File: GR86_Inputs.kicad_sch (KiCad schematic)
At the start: 57 parts, among them U801 74LV1T125, U802 74LV1T125, U803 74LV1T125, U804 74LV1T125, U805 74LV1T125, U806 ES7241D

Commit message: Update .gitignore, CANBus_Interface.kicad_sch, ESP32-S3_WLED_UnderGlow_Hat-2026-05-04_233126.zip, and 17 more files
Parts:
- removed C811, C816: 22uF, My Capacitors:C_0603_Dense, symbol Device:C_Small
- removed C812, C813, C815, C818, C821: 0.1uF, My Capacitors:C_0201_Dense, symbol Device:C_Small
- removed C814, C817, C819, C820, C822: 1uF, My Capacitors:C_0402_Dense, symbol Device:C_Small
- added C811, C816: 22uF, My Capacitors:C_0603_Dense, symbol Device:C
- added C812, C813, C815, C819, C820, C821, C822: 0.1uF, My Capacitors:C_0201_Dense, symbol Device:C
- added C814, C817, C818: 1uF, My Capacitors:C_0201_Dense, symbol Device:C
- C801, C802, C803, C804, C805, C806, C807, C808, C809, C810: symbol Device:C_Small -> Device:C
- R809: value 5k1 -> 33R; Distributor Link 1 https://www.digikey.com/en/products/detail/yageo/AC0201FR-075K1L/5894738 -> https://www.digikey.com/en/products/detail/yageo/AC0201FR-0733RL/5894558; Distributor Link 2 https://www.mouser.com/ProductDetail/YAGEO/AC0201FR-075K1L?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 -> https://www.mouser.com/ProductDetail/YAGEO/AC0201FR-0733RL?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; LCSC C226588 -> C226514; Manufacturer Part Number AC0201FR-075K1L -> AC0201FR-0733RL
- R811: value 33R -> 5k1; Distributor Link 1 https://www.digikey.com/en/products/detail/yageo/AC0201FR-0733RL/5894558 -> https://www.digikey.com/en/products/detail/yageo/AC0201FR-075K1L/5894738; Distributor Link 2 https://www.mouser.com/ProductDetail/YAGEO/AC0201FR-0733RL?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 -> https://www.mouser.com/ProductDetail/YAGEO/AC0201FR-075K1L?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; LCSC C226514 -> C226588; Manufacturer Part Number AC0201FR-0733RL -> AC0201FR-075K1L
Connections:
- net +3V3: now also R811.2, C811.1, C812.1, C813.1, C814.1, C815.1, C816.1; no longer R809.2
- net AUX_{R}: now also R810.2; no longer R811.2
- net SD: now also R811.1; no longer R809.1
- net A_{IN}R: now reaches U806.10 (A_{IN}R)
- net A_{IN}R: now also C818.2
- net REF_{P}: now reaches U806.13 (REF_{P})
- net REF_{P}: now also C819.1, C820.1
- net SD_{OUT}: now reaches R812.2, U806.2 (SD_{OUT})
- net A_{IN}L: now reaches U806.8 (A_{IN}L)
- net A_{IN}L: now also C817.2
- net REF_{Q}: now reaches U806.9 (REF_{Q})
- net REF_{Q}: now also C821.1, C822.1
- net RR_{809-810}: now reaches R810.1
- net RR_{809-810}: now also R809.2
- net RR_{807-808}: now reaches R807.1, R808.2
- net RC_{808-817}: now reaches R808.1
- net RC_{808-817}: now also C817.1
- net AGND renamed GNDA
- net GNDA: now also C811.2, C812.2, C813.2, C814.2, C815.2, C816.2, C819.2, C820.2, C821.2, C822.2
- net ~{Dome_S}: no longer names the net of D813.2 (A), R806.1
- new net RC_{809-818}: C818.1, R809.1
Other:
- moved on the sheet: R806, R813

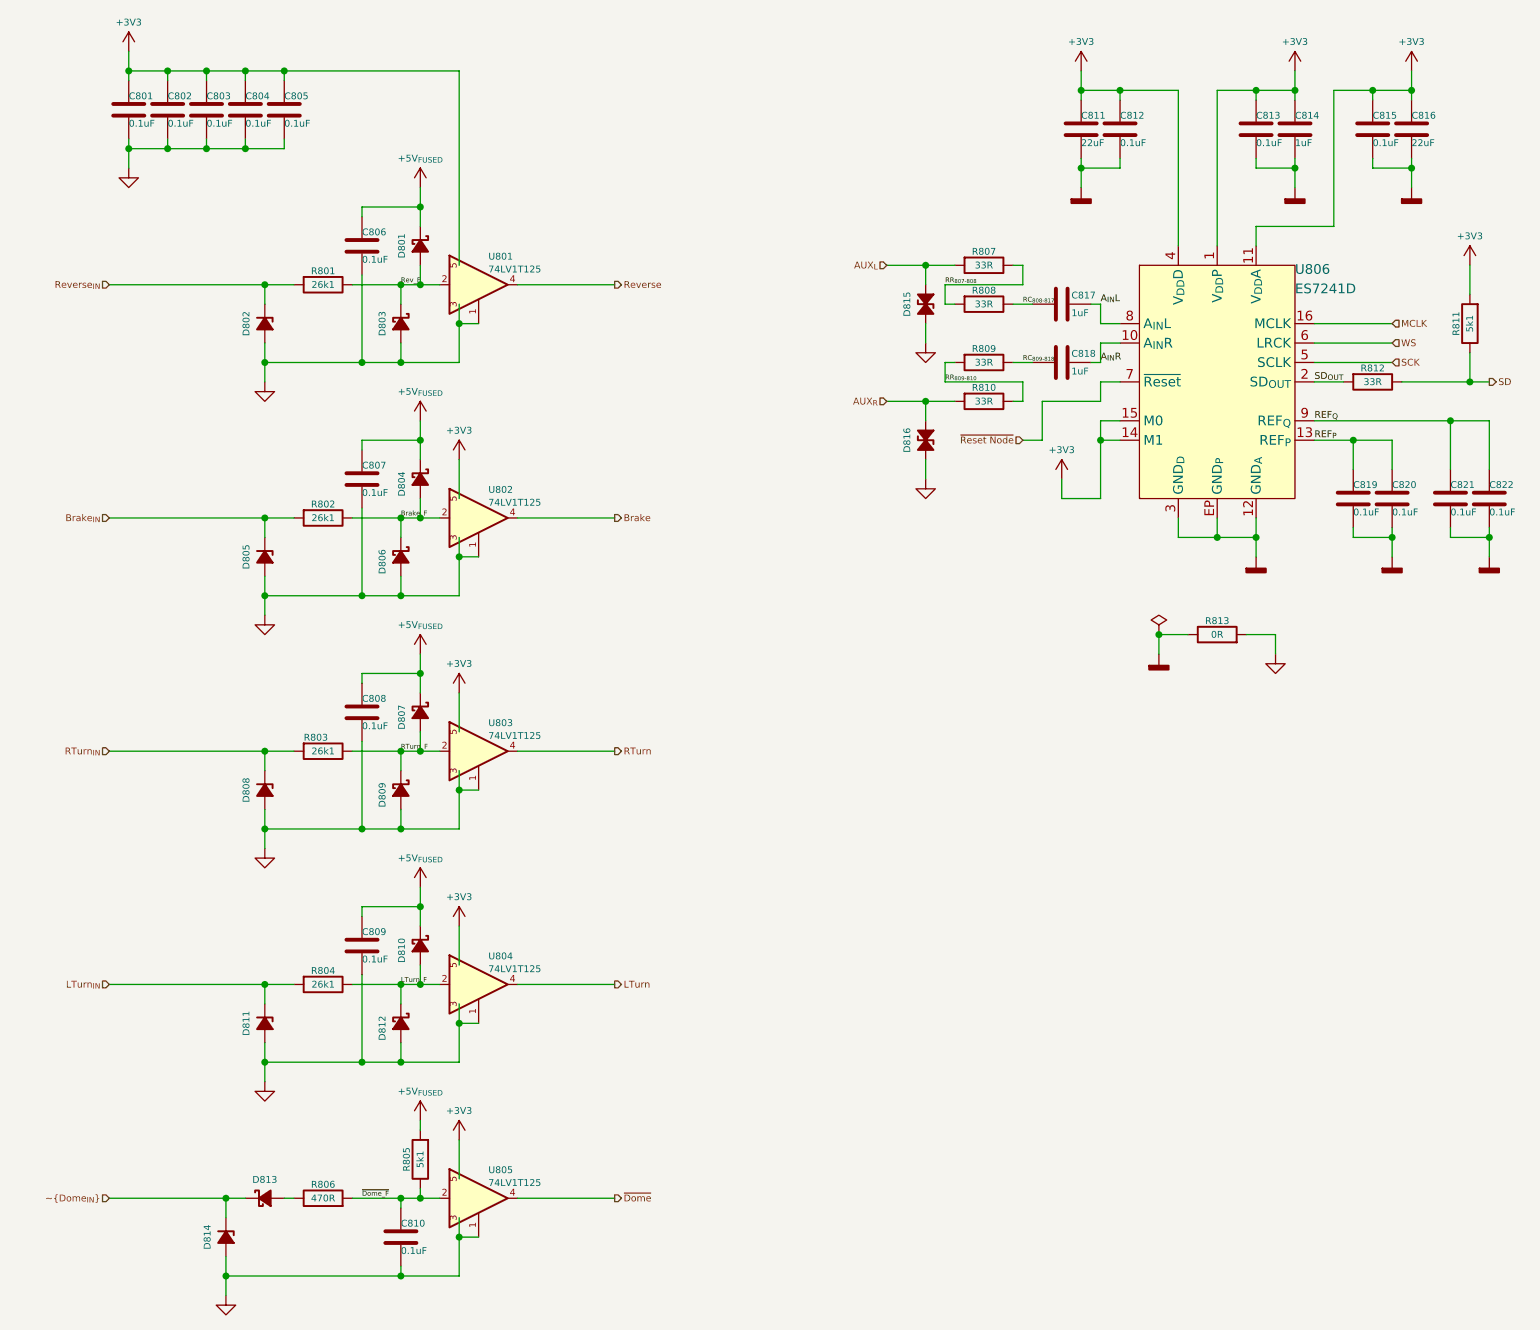
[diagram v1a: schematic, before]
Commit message: replaced Device:C with Device:C_Small and Device:R with Device:R_Small
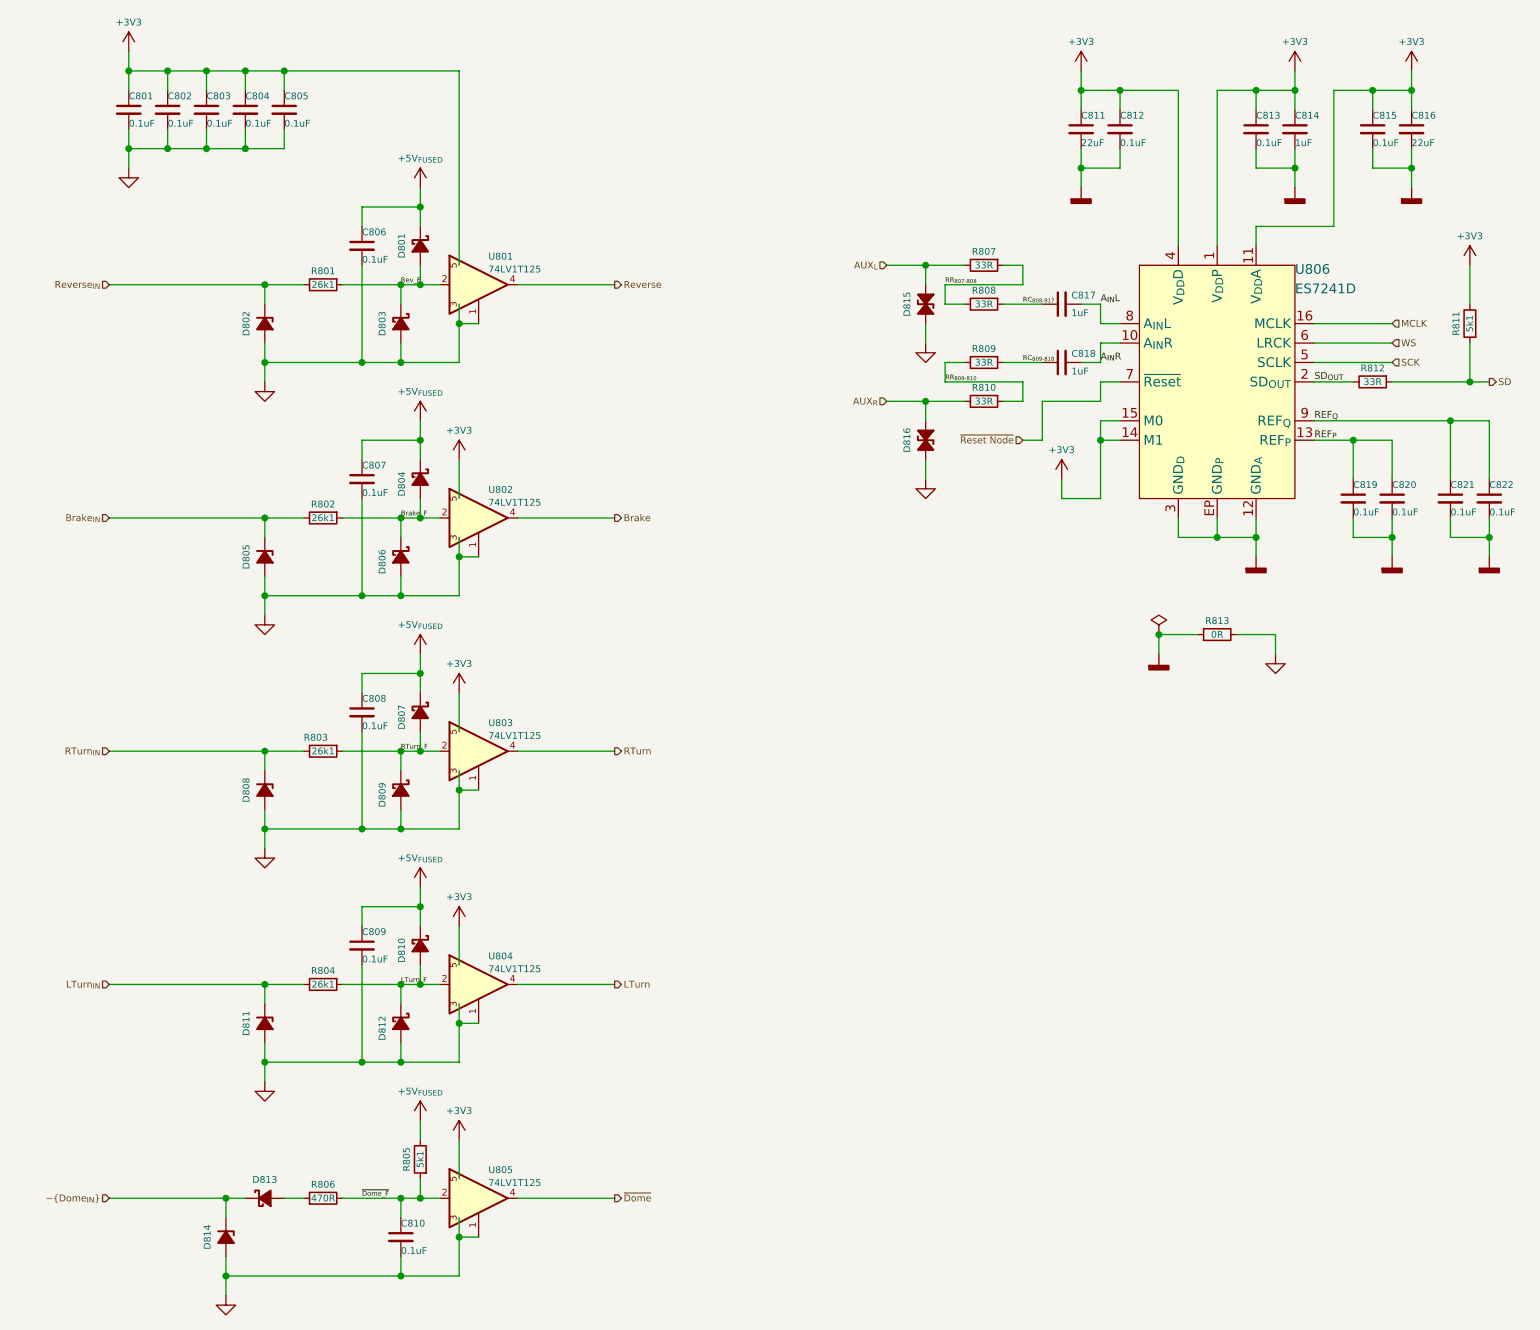
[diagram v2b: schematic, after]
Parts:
- C801, C802, C803, C804, C805, C806, C807, C808, C809, C810, C811, C812, C813, C814, C815, C816, C817, C818, C819, C820, C821, C822: symbol Device:C -> Device:C_Small
- R801, R802, R803, R804, R805, R806, R807, R808, R809, R810, R811, R812, R813: symbol Device:R -> Device:R_Small

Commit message: Updated Net Names for FSPI and I2S nets
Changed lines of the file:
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@@
 	)
 	(label "RC_{808-817}"
-		(at 195.58 53.34 0)
+		(at 193.04 53.34 0)
 		(effects
 			(font
@@
 	)
 	(label "RC_{809-818}"
-		(at 195.58 60.96 0)
+		(at 193.04 60.96 0)
 		(effects
 			(font

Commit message: Update .gitignore, ESP32-S3_WLED_UnderGlow_Hat-2026-05-05_083139.zip, ESP32-S3_WLED_UnderGlow_Hat.kicad_pcb, and 1 more file
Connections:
- net GNDA: now also U806.17 (GND_{P}); no longer U806.EP (GND_{P})
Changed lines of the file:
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@@
 		(pin "5"
 		)
-		(pin "EP"
+		(pin "17"
 		)
 		(pin "16"

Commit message: JLCPCB: W2026061412450502 2026-06-14 PCB: Y62-5297522A PCBA: SMT026061460215-5297522A
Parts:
- added +V20, +V21, +V22, +V23, +V25, +V27, +V28, +V30, +V32, +V34, +V36: +3V3, symbol My Power Management:+V (Local)
- added +V24, +V26, +V29, +V31, +V33, +V35: +5V_{FUSED}, symbol My Power Management:+V (Local)
- added GND18, GND19, GND20, GND21, GND22, GND23, GND24, GND25, GND26, GND27: GND, symbol My Power Management:GND (Local)
- added GNDC1, GNDC2, GNDC3, GNDC4, GNDC5, GNDC6: GND3, symbol My Power Management:GND (chip)
- added GNDC7: GNDC, symbol My Power Management:GND (chip)
- D801, D803, D804, D806, D807, D809, D810, D812, D813: footprint Personal_FootprintLibrary:DSN0603-2 -> My Package_Leadless:DFN0603-2
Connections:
- net +3V3: now also +V20.1, +V21.1, +V22.1, +V23.1, +V25.1, +V27.1, +V28.1, +V30.1, +V32.1, +V34.1, +V36.1
- net +5V_{FUSED}: now also +V24.1, +V26.1, +V29.1, +V31.1, +V33.1, +V35.1
- net GND: now also GND18.1 (GND), GND19.1 (GND), GND20.1 (GND), GND21.1 (GND), GND22.1 (GND), GND23.1 (GND), GND24.1 (GND), GND25.1 (GND), GND26.1 (GND), GND27.1 (GND)
- net GNDA renamed GND3
- net GND3: now also GNDC1.1 (GND_{chip}), GNDC2.1 (GND_{chip}), GNDC3.1 (GND_{chip}), GNDC4.1 (GND_{chip}), GNDC5.1 (GND_{chip}), GNDC6.1 (GND_{chip}), GNDC7.1 (GND_{chip})
